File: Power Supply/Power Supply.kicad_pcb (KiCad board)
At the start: 2 copper layers, 127 x 101.6 mm, 36 parts, among them J1 Conn_01x01_Female, J2 Conn_01x01_Female, J3 Conn_01x01_Female, J4 Conn_01x01_Female, J5 Conn_01x01_Female, U1 LM337_TO220, U2 LM317_3PinPackage

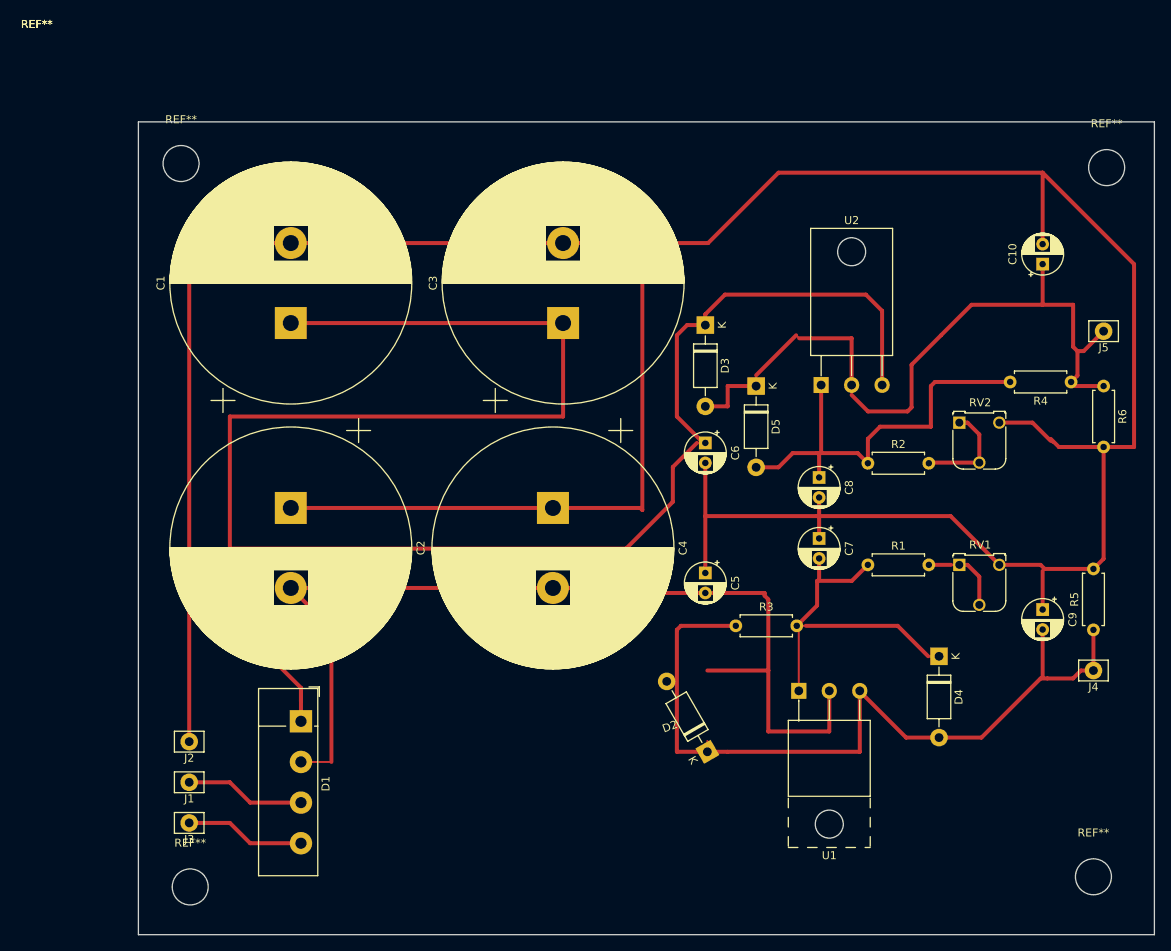
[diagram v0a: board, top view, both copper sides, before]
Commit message: cleaned up pcb, fixed bridge rectifier pinout, added silkscreen and exported fabrication files
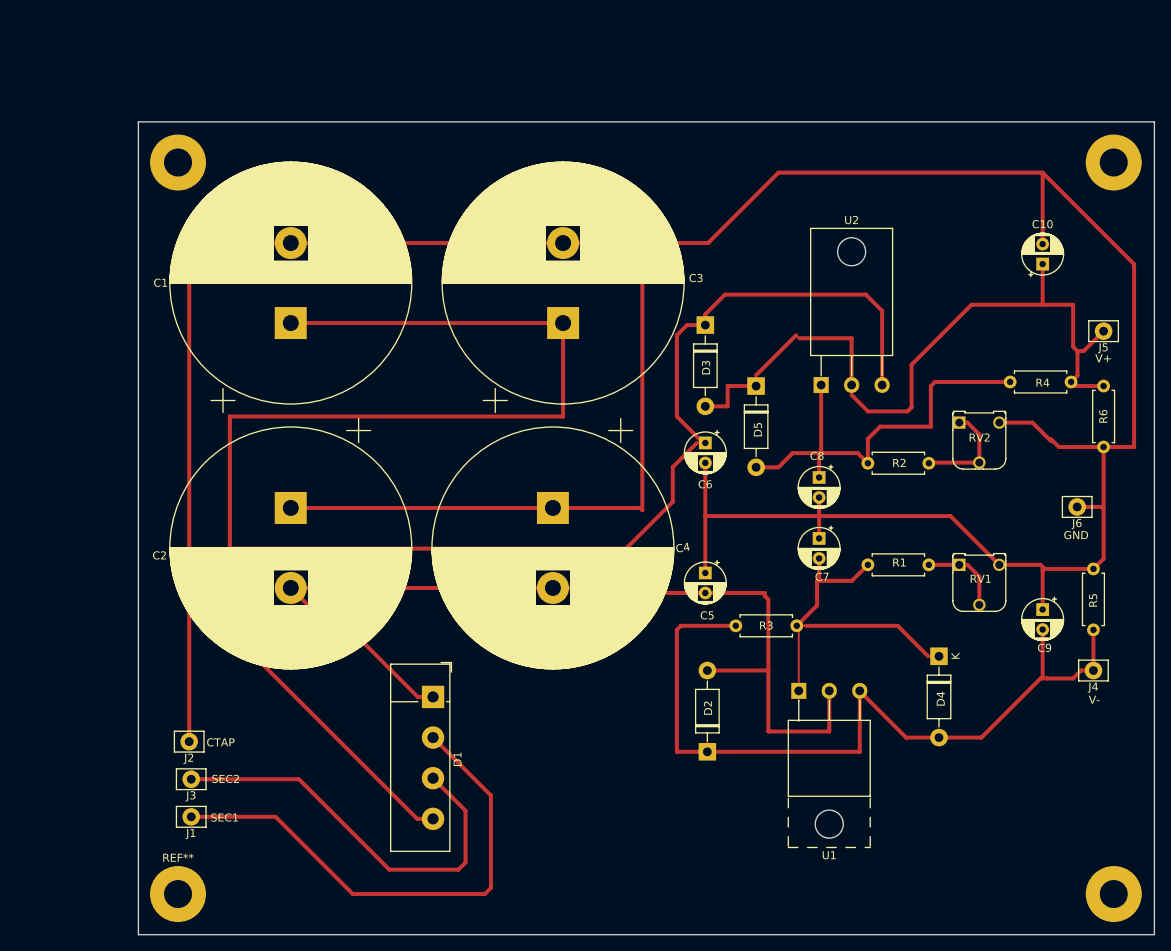
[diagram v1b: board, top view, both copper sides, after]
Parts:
- removed the REF** at (19.2, 108.3)
- removed the REF** at (18.0, 17.9)
- removed the REF** at (133.7, 18.4)
- removed the REF** at (132.1, 107.1)
- added J6: GND_Conn, Connector_Pin:Pin_D1.1mm_L10.2mm_W3.5mm_Flat, F.Cu at (130.0, 60.8)
- added REF**: MountingHole_3.5mm_Pad, MountingHole:MountingHole_3.5mm_Pad, F.Cu at (134.6, 17.8)
- added REF**: MountingHole_3.5mm_Pad, MountingHole:MountingHole_3.5mm_Pad, F.Cu at (134.6, 109.2)
- added REF**: MountingHole_3.5mm_Pad, MountingHole:MountingHole_3.5mm_Pad, F.Cu at (17.7, 109.2)
- added REF**: MountingHole_3.5mm_Pad, MountingHole:MountingHole_3.5mm_Pad, F.Cu at (17.7, 17.8)
- J4: value Conn_01x01_Female -> -V_Conn
- J5: value Conn_01x01_Female -> +V_Conn
- moved D1 16.8 mm to (49.5, 84.6)
- moved J3 5.47 mm to (19.3, 94.9)
- moved J1 4.33 mm to (19.3, 99.6)
- turned D2 to 90 degrees
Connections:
- net /VPOS renamed Net-(C10-Pad1)
- D1 pad 1: Net-(C1-Pad1) -> Net-(C2-Pad2)
- D1 pad 2: Net-(C2-Pad2) -> /SEC1
- D1 pad 3: /SEC1 -> Net-(D1-Pad3)
- D1 pad 4: Net-(D1-Pad4) -> Net-(C1-Pad1)
- J3 pad 1: Net-(D1-Pad4) -> Net-(D1-Pad3)
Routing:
- net Net-(D1-Pad3): track 0.00 -> 51.6 mm
- net /SEC1: track 15.0 -> 63.6 mm
- net Net-(C1-Pad1): track 251.6 -> 271.2 mm
- net Net-(D1-Pad4): track 15.8 -> 0.00 mm
- net Net-(C2-Pad2): track 125.6 -> 120.8 mm
- net Earth: track 408.1 -> 412.0 mm
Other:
- board text added: "CTAP"
- board text added: "GND"
- board text added: "SEC1"
- board text added: "SEC2"
- board text added: "V+"
- board text added: "V-"
